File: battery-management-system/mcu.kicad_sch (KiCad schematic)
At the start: 28 parts, among them J11 I2C, J12 MCU_SUPPLY, J13 LEDS, U4 STM32L071CZTx, U5 ARM-JTAG-SWD, U8 AT24C512C, U9 NCT75DR2G

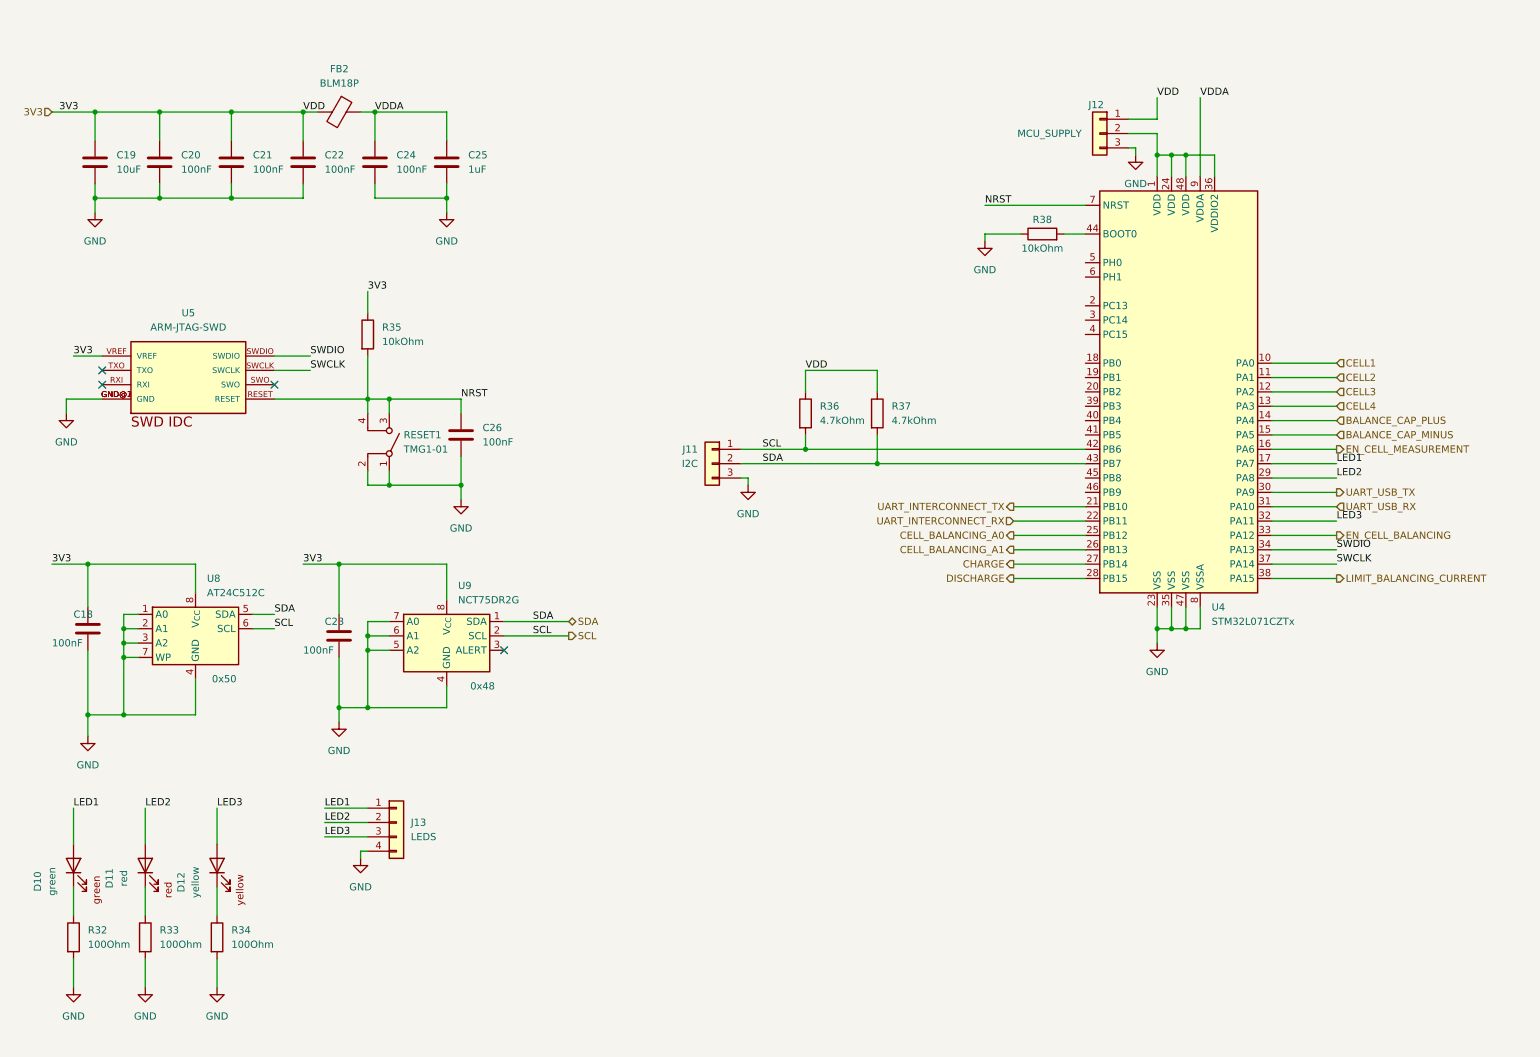
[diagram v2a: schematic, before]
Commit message: implement balancing
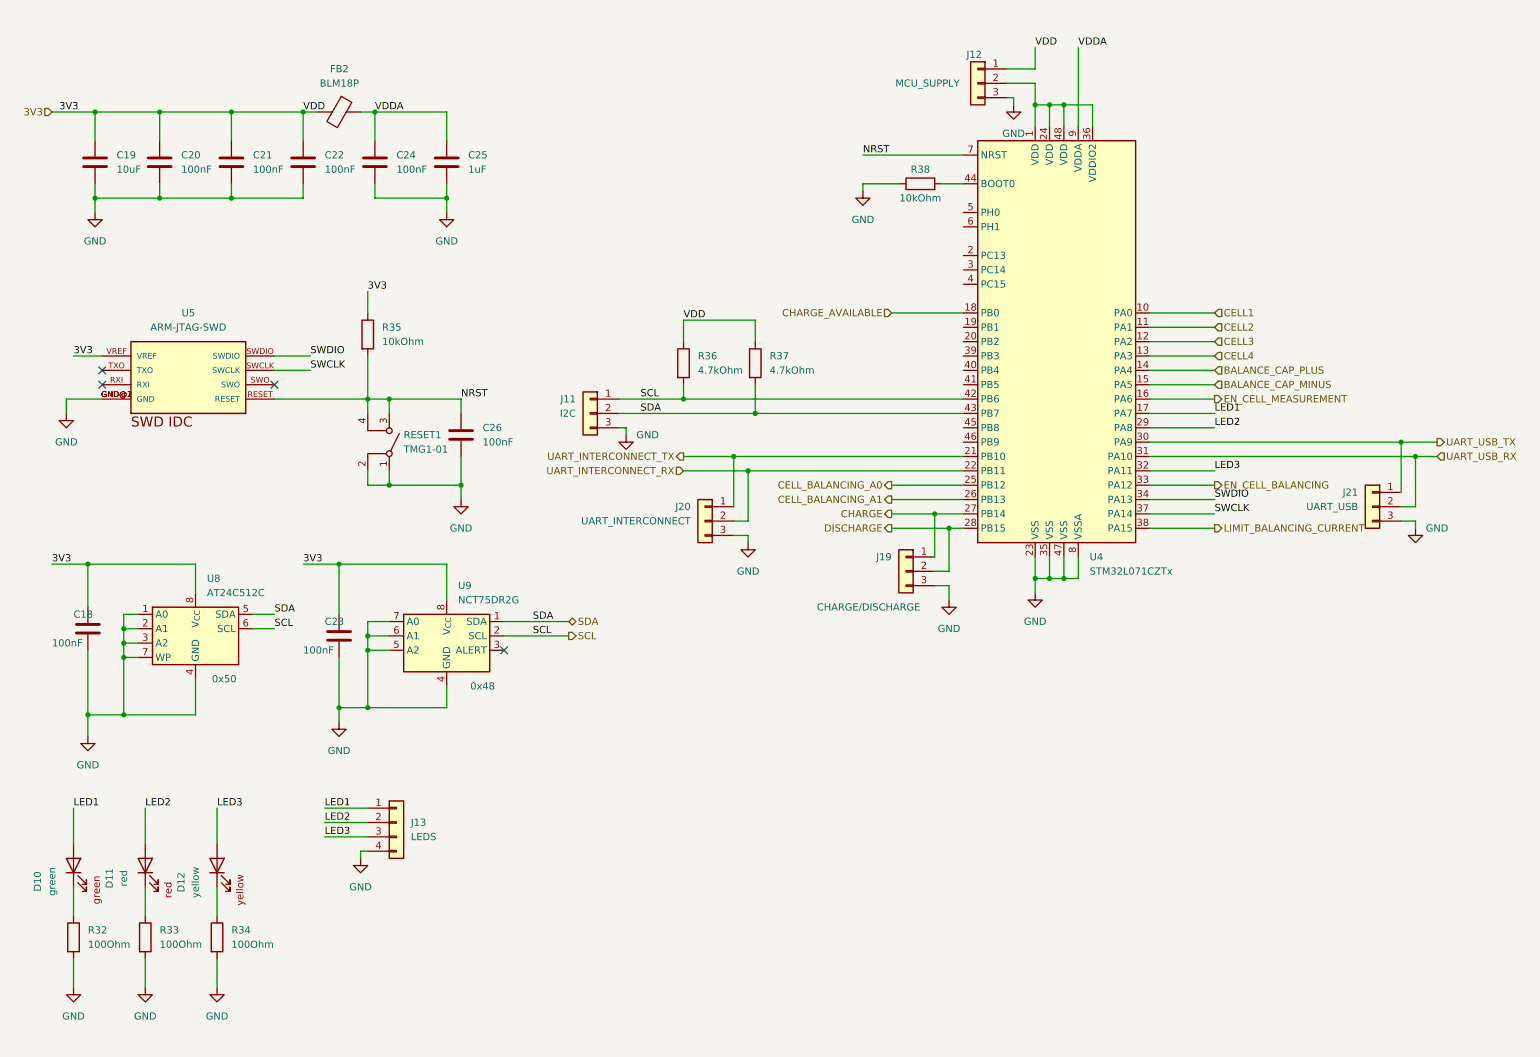
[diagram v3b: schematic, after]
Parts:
- added J19: CHARGE/DISCHARGE, benediktibk:PinHeader_1x03_P2.54mm_Vertical, symbol benediktibk:Conn_01x03
- added J20: UART_INTERCONNECT, benediktibk:PinHeader_1x03_P2.54mm_Vertical, symbol benediktibk:Conn_01x03
- added J21: UART_USB, benediktibk:PinHeader_1x03_P2.54mm_Vertical, symbol benediktibk:Conn_01x03
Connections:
- net CHARGE: now also J19.1 (Pin_1)
- net DISCHARGE: now also J19.2 (Pin_2)
- net GND: now also J19.3 (Pin_3), J20.3 (Pin_3), J21.3 (Pin_3)
- net UART_INTERCONNECT_RX: now also J20.2 (Pin_2)
- net UART_INTERCONNECT_TX: now also J20.1 (Pin_1)
- net UART_USB_RX: now also J21.2 (Pin_2)
- net UART_USB_TX: now also J21.1 (Pin_1)
- net CHARGE_AVAILABLE: now reaches U4.18 (PB0)
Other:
- moved on the sheet: J11, J12, R36, R37, R38, U4

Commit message: add fuel gauge IC
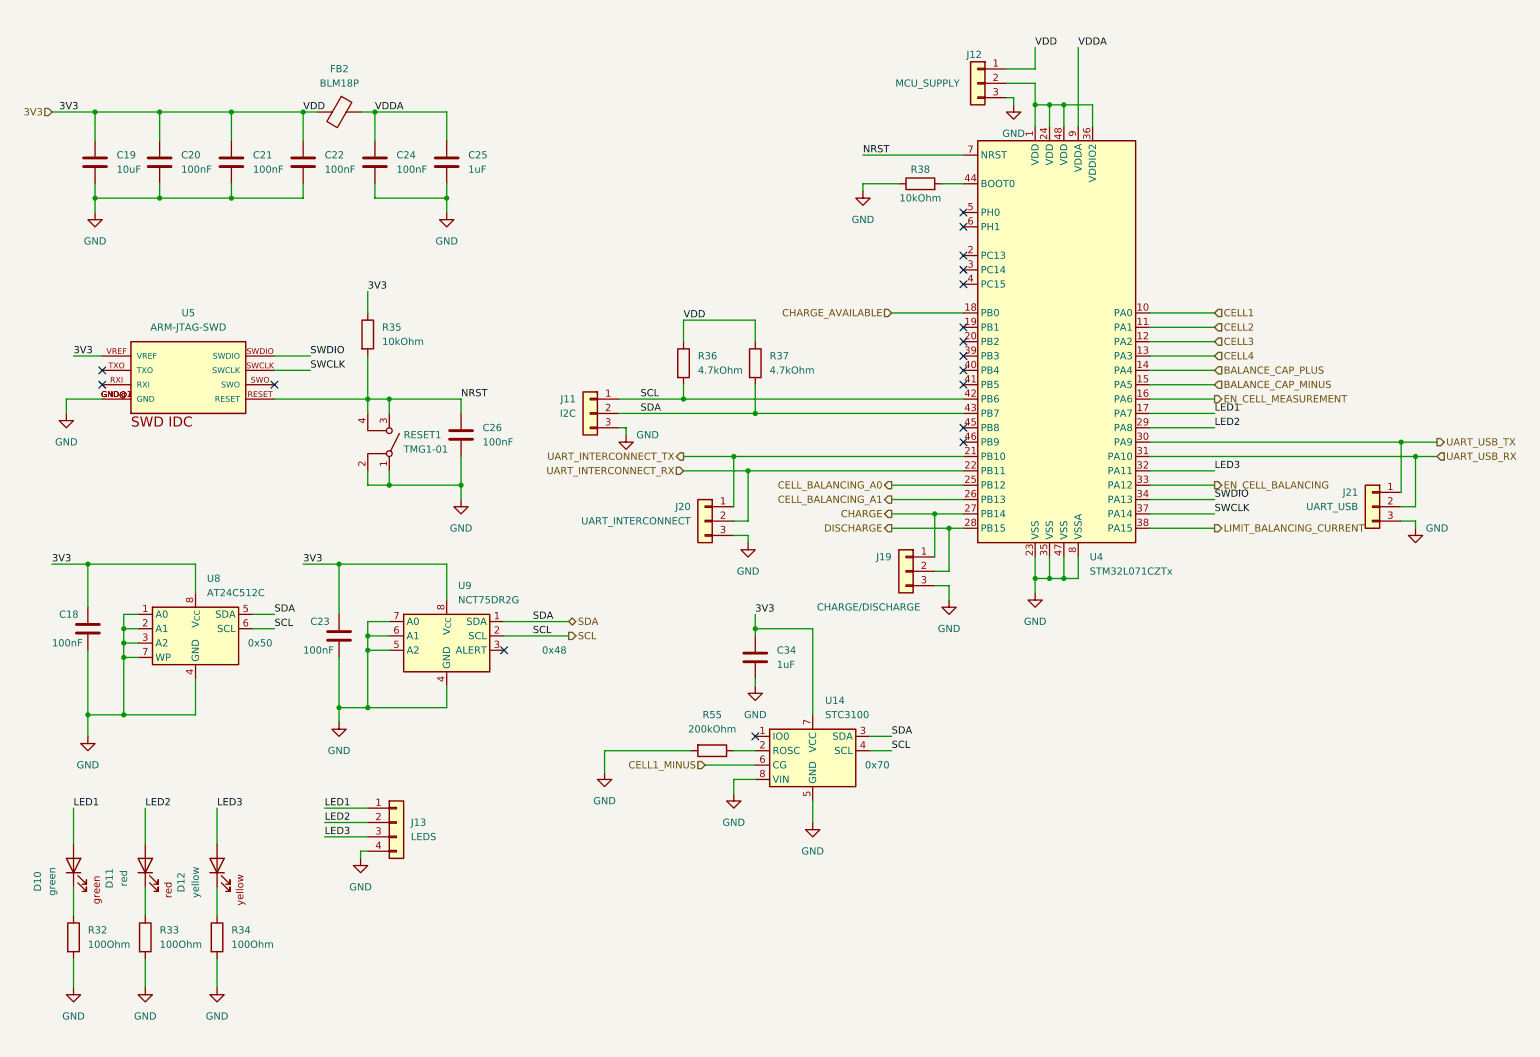
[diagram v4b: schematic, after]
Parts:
- added C34: 1uF, benediktibk:C_0603_1608Metric_Pad1.08x0.95mm_HandSolder, symbol benediktibk:C_1uF_SMD_0603_50V_10%
- added R55: 200kOhm, benediktibk:R_0603_1608Metric_Pad0.98x0.95mm_HandSolder, symbol benediktibk:R_200kOhm_SMD_0603_30mW_0_1%
- added U14: STC3100, benediktibk:MSOP-8_3x3mm_P0.65mm, symbol benediktibk:STC3100
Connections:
- net 3V3: now also C34.1, U14.7 (VCC)
- net GND: now also C34.2, R55.2, U14.5 (GND), U14.8 (VIN)
- net SCL: now also U14.4 (SCL)
- net SDA: now also U14.3 (SDA)
- new net: R55.1, U14.2 (ROSC)
- new net CELL1_MINUS: U14.6 (CG)
- no-connect marks 4 -> 17

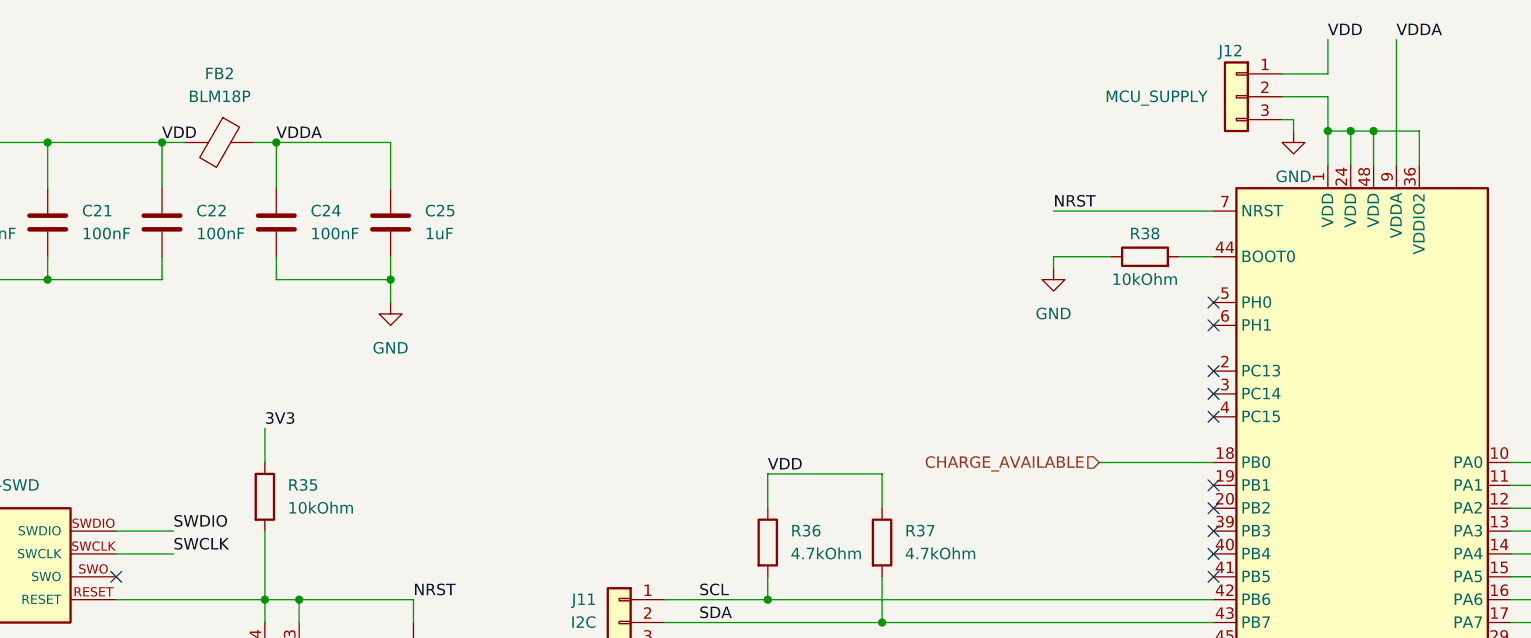
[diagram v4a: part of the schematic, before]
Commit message: fix electrical rule checker errors
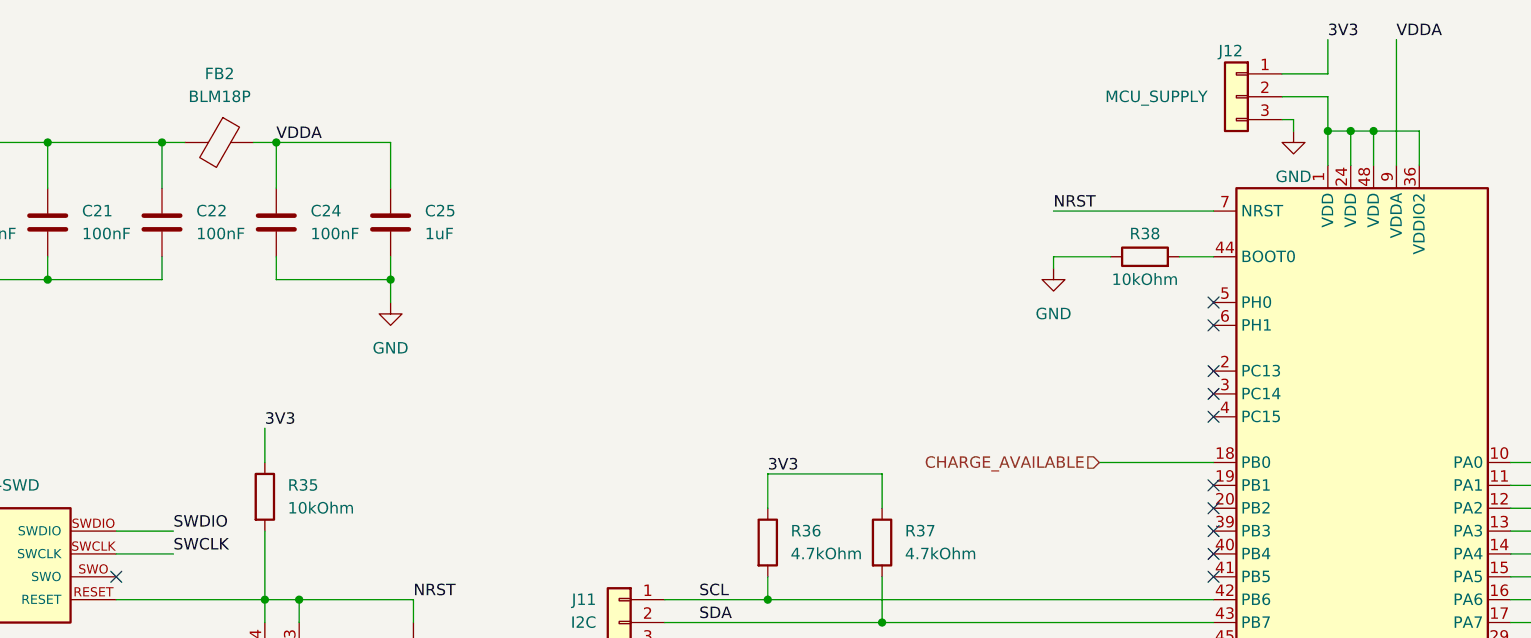
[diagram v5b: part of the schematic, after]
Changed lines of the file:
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@@
     (stroke (width 0) (type default))
+  )
+  (label "3V3" (at 135.89 67.31 0) (fields_autoplaced)
+    (effects (font (size 1.27 1.27)) (justify left bottom))
   )
   (label "LED3" (at 53.34 153.67 0) (fields_autoplaced)
@@
   )
   (label "3V3" (at 68.58 110.49 0) (fields_autoplaced)
+    (effects (font (size 1.27 1.27)) (justify left bottom))
+  )
+  (label "3V3" (at 198.12 19.05 0) (fields_autoplaced)
     (effects (font (size 1.27 1.27)) (justify left bottom))
   )
@@
     (effects (font (size 1.27 1.27)) (justify left bottom))
   )
-  (label "VDD" (at 198.12 19.05 0) (fields_autoplaced)
-    (effects (font (size 1.27 1.27)) (justify left bottom))
-  )
   (label "3V3" (at 80.01 62.23 0) (fields_autoplaced)
     (effects (font (size 1.27 1.27)) (justify left bottom))
@@
     (effects (font (size 1.27 1.27)) (justify left bottom))
   )
-  (label "VDD" (at 68.58 30.48 0) (fields_autoplaced)
-    (effects (font (size 1.27 1.27)) (justify left bottom))
-  )
   (label "SWDIO" (at 229.87 99.06 0) (fields_autoplaced)
     (effects (font (size 1.27 1.27)) (justify left bottom))
@@
     (effects (font (size 1.27 1.27)) (justify left bottom))
   )
-  (label "VDD" (at 135.89 67.31 0) (fields_autoplaced)
-    (effects (font (size 1.27 1.27)) (justify left bottom))
-  )
